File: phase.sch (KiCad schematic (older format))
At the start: 30 parts, among them U4 INA240A1PW, U5 UCC21520DW

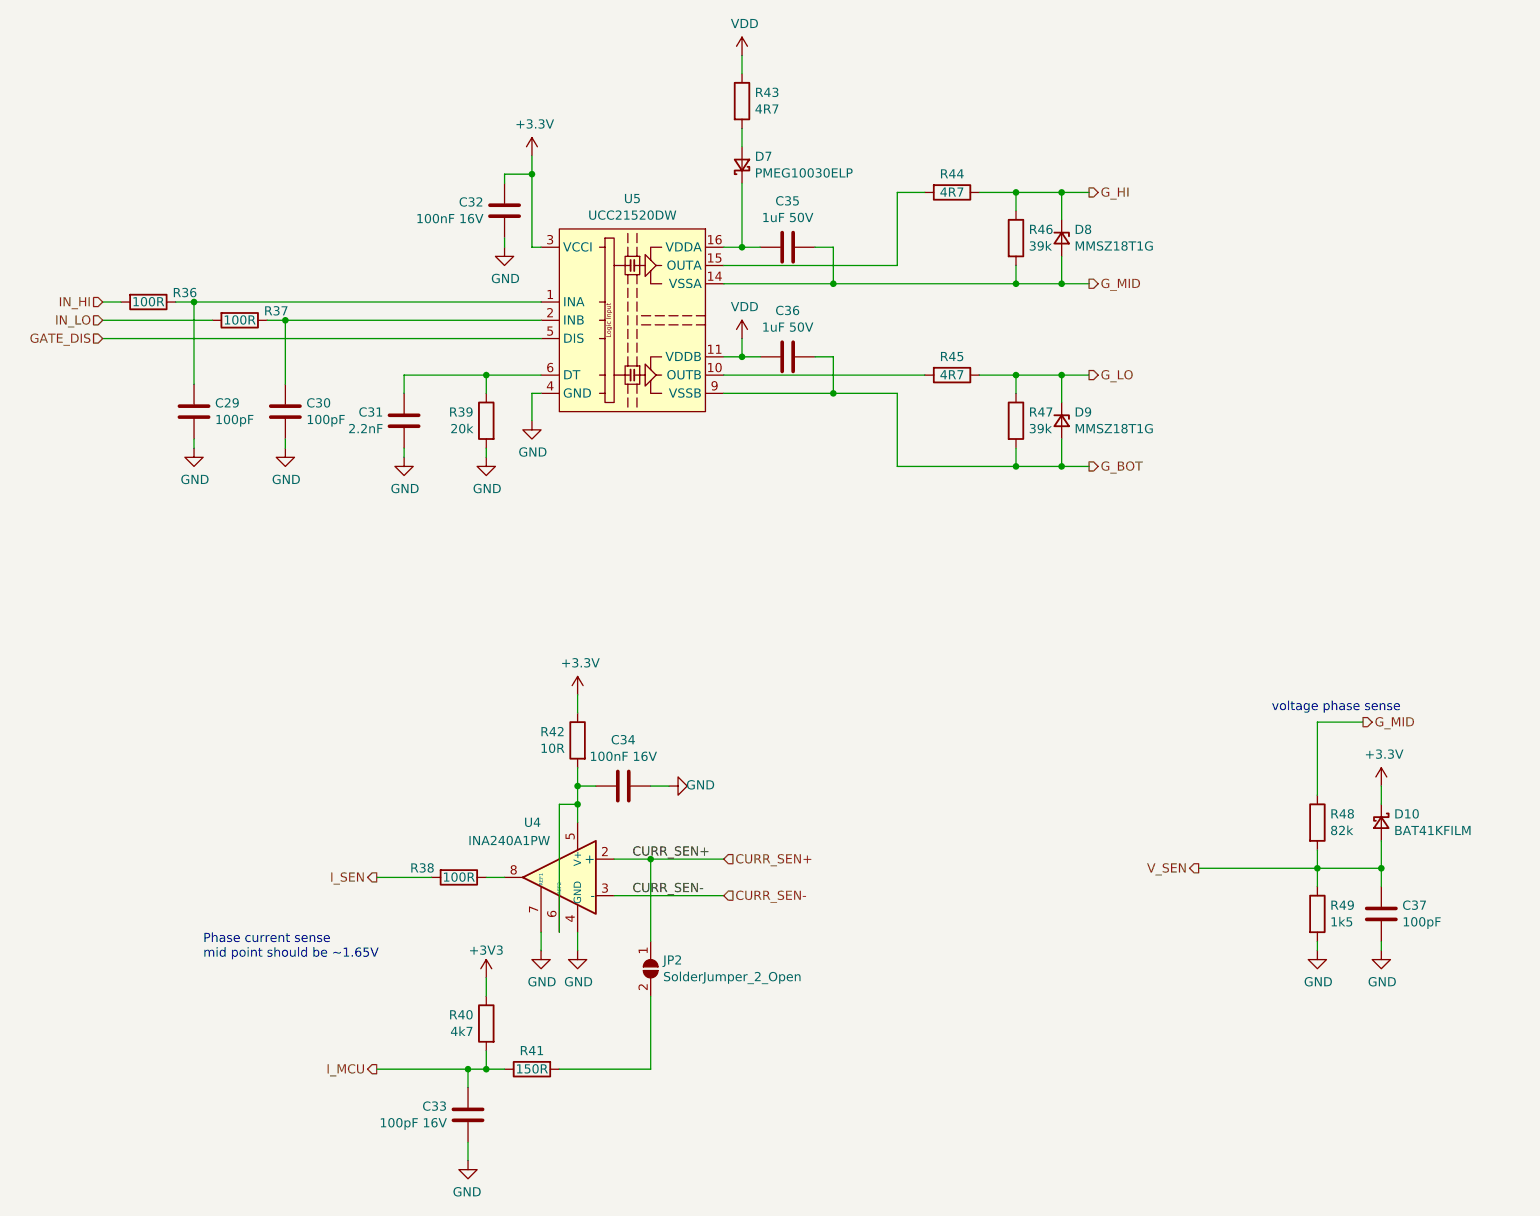
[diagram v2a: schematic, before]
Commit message: Adding 0V TP and labels
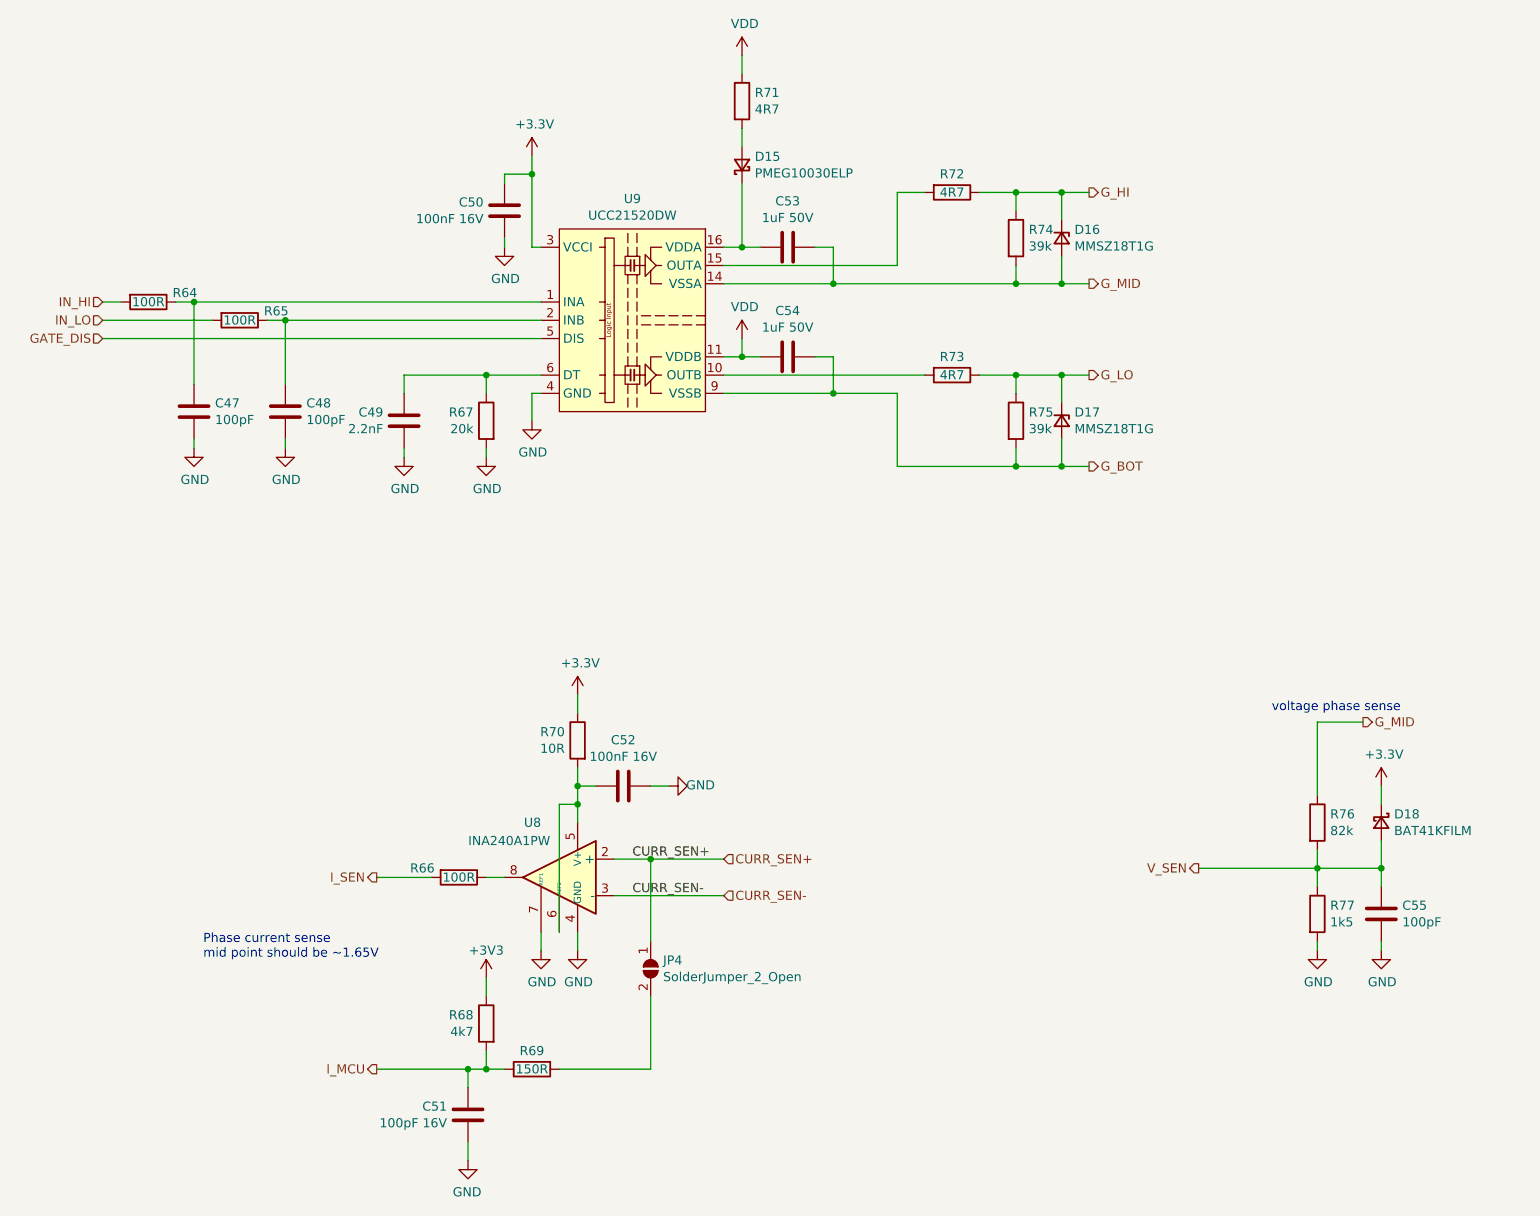
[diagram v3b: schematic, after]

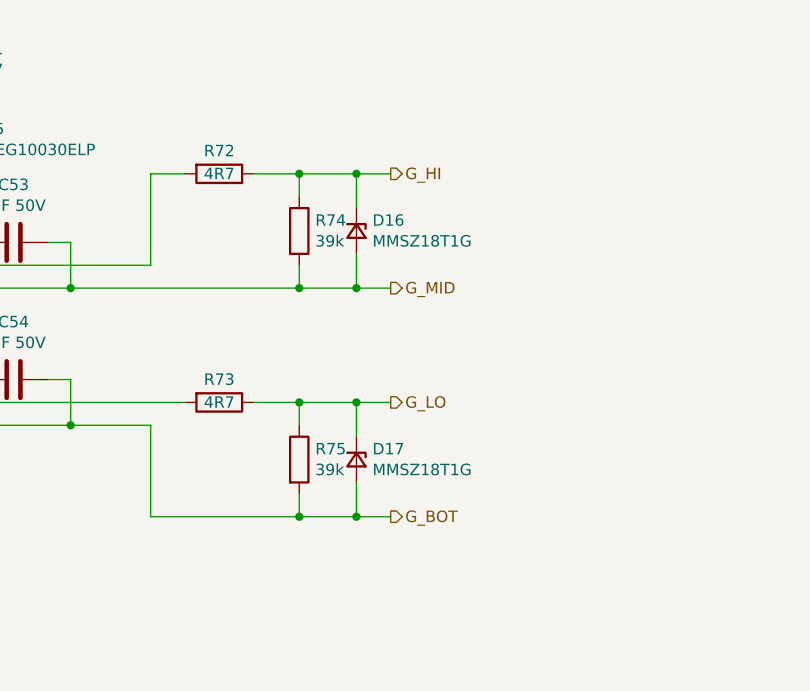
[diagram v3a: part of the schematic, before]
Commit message: upgrading to 4layer
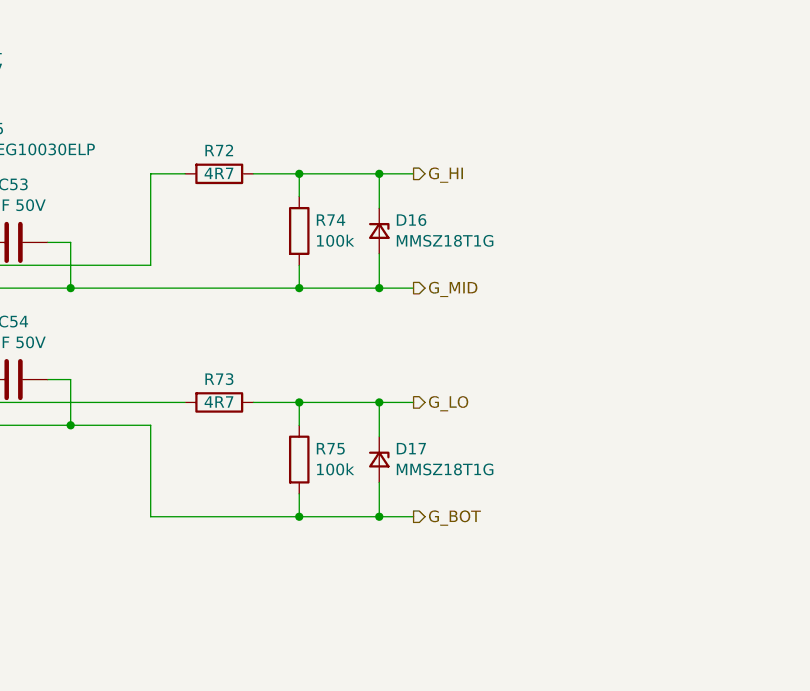
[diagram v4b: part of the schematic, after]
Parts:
- R46, R47: value 39k -> 100k; LCSC C25783 -> C25741
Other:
- moved on the sheet: D16, D17
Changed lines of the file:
@@
 $Descr A4 11693 8268
 encoding utf-8
-Sheet 3 5
+Sheet 4 5
 Title "MESC_IMS_Ctrl"
 Date "2021-04-10"
@@
 Text Notes 9200 4600 0    50   ~ 0
 voltage phase sense
-Text HLabel 8200 2250 2    50   Output ~ 0
+Text HLabel 8300 2250 2    50   Output ~ 0
 G_MID
-Text HLabel 8200 2750 2    50   Output ~ 0
+Text HLabel 8300 2750 2    50   Output ~ 0
 G_LO
 Text HLabel 6200 5400 2    50   Input ~ 0
@@
 Text HLabel 6200 5600 2    50   Input ~ 0
 CURR_SEN-
-Text HLabel 8200 1750 2    50   Output ~ 0
+Text HLabel 8300 1750 2    50   Output ~ 0
 G_HI
 $Comp
@@
 L Device:D_Zener_Small D8
 U 1 1 60817438
-P 8050 2000
+P 8150 2000
 AR Path="/6070CE7F/60817438" Ref="D8"  Part="1"
 AR Path="/6074FE4E/60817438" Ref="D12"  Part="1"
 AR Path="/6075047A/60817438" Ref="D16"  Part="1"
-F 0 "D16" V 8004 2070 50  0000 L CNN
-F 1 "MMSZ18T1G" V 8095 2070 50  0000 L CNN
-F 2 "Diode_SMD:D_SOD-123" V 8050 2000 50  0001 C CNN
-F 3 "~" V 8050 2000 50  0001 C CNN
-F 4 "C382948" H 8050 2000 50  0001 C CNN "LCSC"
-F 5 "Yes" H 8050 2000 50  0001 C CNN "Checked"
-	1    8050 2000
+F 0 "D16" V 8104 2070 50  0000 L CNN
+F 1 "MMSZ18T1G" V 8195 2070 50  0000 L CNN
+F 2 "Diode_SMD:D_SOD-123" V 8150 2000 50  0001 C CNN
+F 3 "~" V 8150 2000 50  0001 C CNN
+F 4 "C382948" H 8150 2000 50  0001 C CNN "LCSC"
+F 5 "Yes" H 8150 2000 50  0001 C CNN "Checked"
+	1    8150 2000
 	0    1    1    0
 $EndComp
@@
 L Device:D_Zener_Small D9
 U 1 1 60818839
-P 8050 3000
+P 8150 3000
 AR Path="/6070CE7F/60818839" Ref="D9"  Part="1"
 AR Path="/6074FE4E/60818839" Ref="D13"  Part="1"
 AR Path="/6075047A/60818839" Ref="D17"  Part="1"
-F 0 "D17" V 8004 3070 50  0000 L CNN
-F 1 "MMSZ18T1G" V 8095 3070 50  0000 L CNN
-F 2 "Diode_SMD:D_SOD-123" V 8050 3000 50  0001 C CNN
-F 3 "~" V 8050 3000 50  0001 C CNN
-F 4 "C382948" H 8050 3000 50  0001 C CNN "LCSC"
-F 5 "Yes" H 8050 3000 50  0001 C CNN "Checked"
-	1    8050 3000
+F 0 "D17" V 8104 3070 50  0000 L CNN
+F 1 "MMSZ18T1G" V 8195 3070 50  0000 L CNN
+F 2 "Diode_SMD:D_SOD-123" V 8150 3000 50  0001 C CNN
+F 3 "~" V 8150 3000 50  0001 C CNN
+F 4 "C382948" H 8150 3000 50  0001 C CNN "LCSC"
+F 5 "Yes" H 8150 3000 50  0001 C CNN "Checked"
+	1    8150 3000
 	0    1    1    0
 $EndComp
@@
 AR Path="/6075047A/60818EA3" Ref="R75"  Part="1"
 F 0 "R75" H 7870 3046 50  0000 L CNN
-F 1 "39k" H 7870 2955 50  0000 L CNN
+F 1 "100k" H 7870 2955 50  0000 L CNN
 F 2 "Resistor_SMD:R_0402_1005Metric" V 7730 3000 50  0001 C CNN
 F 3 "~" H 7800 3000 50  0001 C CNN
-F 4 "C25783" H 7800 3000 50  0001 C CNN "LCSC"
+F 4 "C25741" H 7800 3000 50  0001 C CNN "LCSC"
 F 5 "Yes" H 7800 3000 50  0001 C CNN "Checked"
 	1    7800 3000
@@
 AR Path="/6075047A/608196FD" Ref="R74"  Part="1"
 F 0 "R74" H 7870 2046 50  0000 L CNN
-F 1 "39k" H 7870 1955 50  0000 L CNN
+F 1 "100k" H 7870 1955 50  0000 L CNN
 F 2 "Resistor_SMD:R_0402_1005Metric" V 7730 2000 50  0001 C CNN
 F 3 "~" H 7800 2000 50  0001 C CNN
-F 4 "C25783" H 7800 2000 50  0001 C CNN "LCSC"
+F 4 "C25741" H 7800 2000 50  0001 C CNN "LCSC"
 F 5 "Yes" H 7800 2000 50  0001 C CNN "Checked"
 	1    7800 2000
@@
 $EndComp
 Wire Wire Line
-	8050 2100 8050 2250
+	8150 2100 8150 2250
 Wire Wire Line
 	7800 2850 7800 2750
 Wire Wire Line
-	8050 2750 8050 2900
+	8150 2750 8150 2900
 Wire Wire Line
 	7800 1850 7800 1750
 Wire Wire Line
-	8050 1750 8050 1900
+	8150 1750 8150 1900
 Wire Wire Line
 	7800 2150 7800 2250
 Wire Wire Line
-	8200 2250 8050 2250
+	8300 2250 8150 2250
 Wire Wire Line
 	7800 3150 7800 3250
 Wire Wire Line
-	8050 3100 8050 3250
+	8150 3100 8150 3250
 $Comp
 L Device:C C35
@@
 Wire Wire Line
 	6200 5600 5600 5600
-Text HLabel 8200 3250 2    50   Output ~ 0
+Text HLabel 8300 3250 2    50   Output ~ 0
 G_BOT
 Wire Wire Line
-	8200 3250 8050 3250
+	8300 3250 8150 3250
 $Comp
 L Device:C C36
@@
 Wire Wire Line
 	6300 1100 6300 1000
-Connection ~ 7800 1750
-Wire Wire Line
-	7800 1750 8050 1750
-Connection ~ 7800 2250
-Connection ~ 8050 1750
-Wire Wire Line
-	8050 1750 8200 1750
-Connection ~ 8050 2250
-Wire Wire Line
-	8050 2250 7800 2250
+Wire Wire Line
+	7800 1750 8150 1750
+Connection ~ 8150 1750
+Wire Wire Line
+	8150 1750 8300 1750
+Connection ~ 8150 2250
+Wire Wire Line
+	8150 2250 7800 2250
 Wire Wire Line
 	7150 1750 7300 1750
 Wire Wire Line
 	6800 2250 7800 2250
-Connection ~ 7800 2750
-Wire Wire Line
-	7800 2750 8050 2750
-Connection ~ 7800 3250
-Connection ~ 8050 2750
-Wire Wire Line
-	8050 2750 8200 2750
-Connection ~ 8050 3250
-Wire Wire Line
-	8050 3250 7800 3250
+Wire Wire Line
+	7800 2750 8150 2750
+Connection ~ 8150 2750
+Wire Wire Line
+	8150 2750 8300 2750
+Connection ~ 8150 3250
+Wire Wire Line
+	8150 3250 7800 3250
 Wire Wire Line
 	6200 2750 7300 2750
@@
 Wire Wire Line
 	5800 5850 5800 5400
+Connection ~ 7800 2250
+Connection ~ 7800 1750
+Connection ~ 7800 2750
+Connection ~ 7800 3250
 $EndSCHEMATC
